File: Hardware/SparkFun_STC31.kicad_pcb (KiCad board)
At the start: 2 copper layers, 25.4 x 25.4 mm, 43 parts, among them J3 Qwiic_RA, J4 I2C, J5 Qwiic_RA, U1 VEML7700-TT

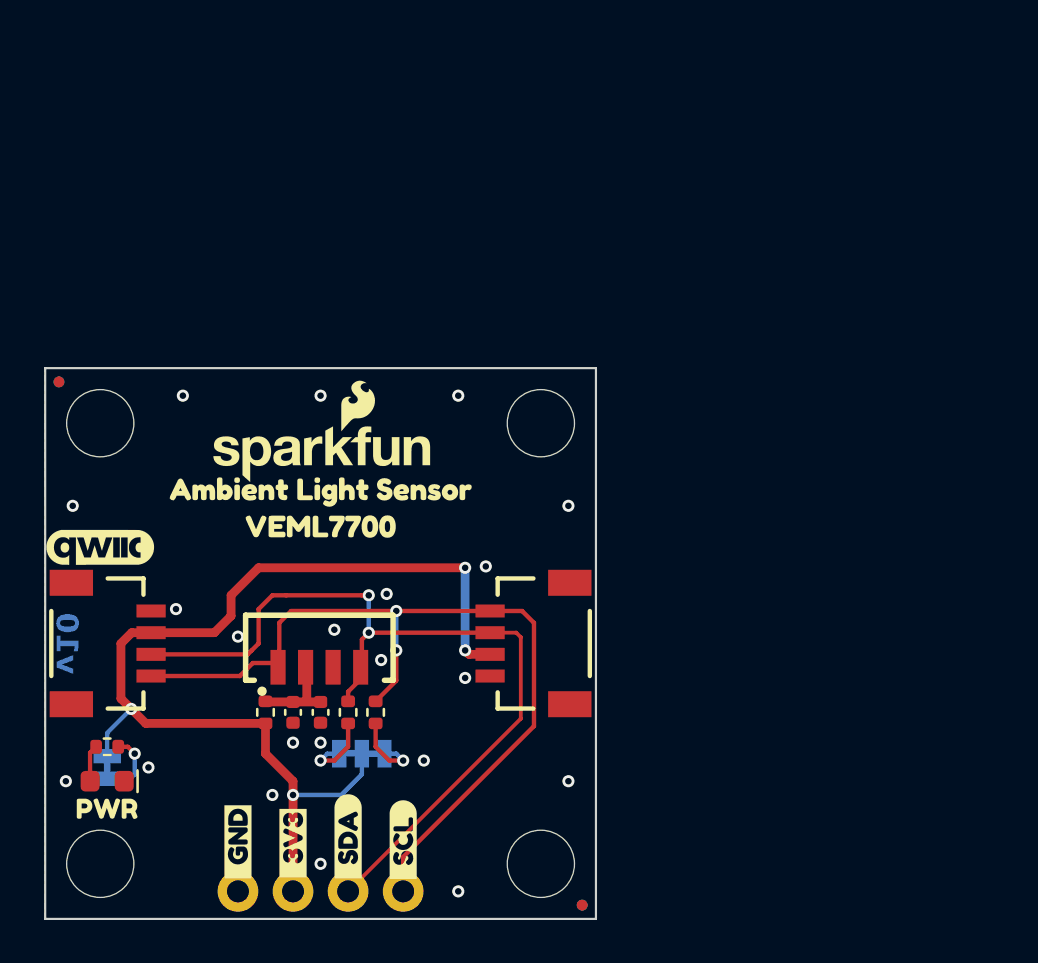
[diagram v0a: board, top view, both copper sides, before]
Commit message: Cleans out the PCB
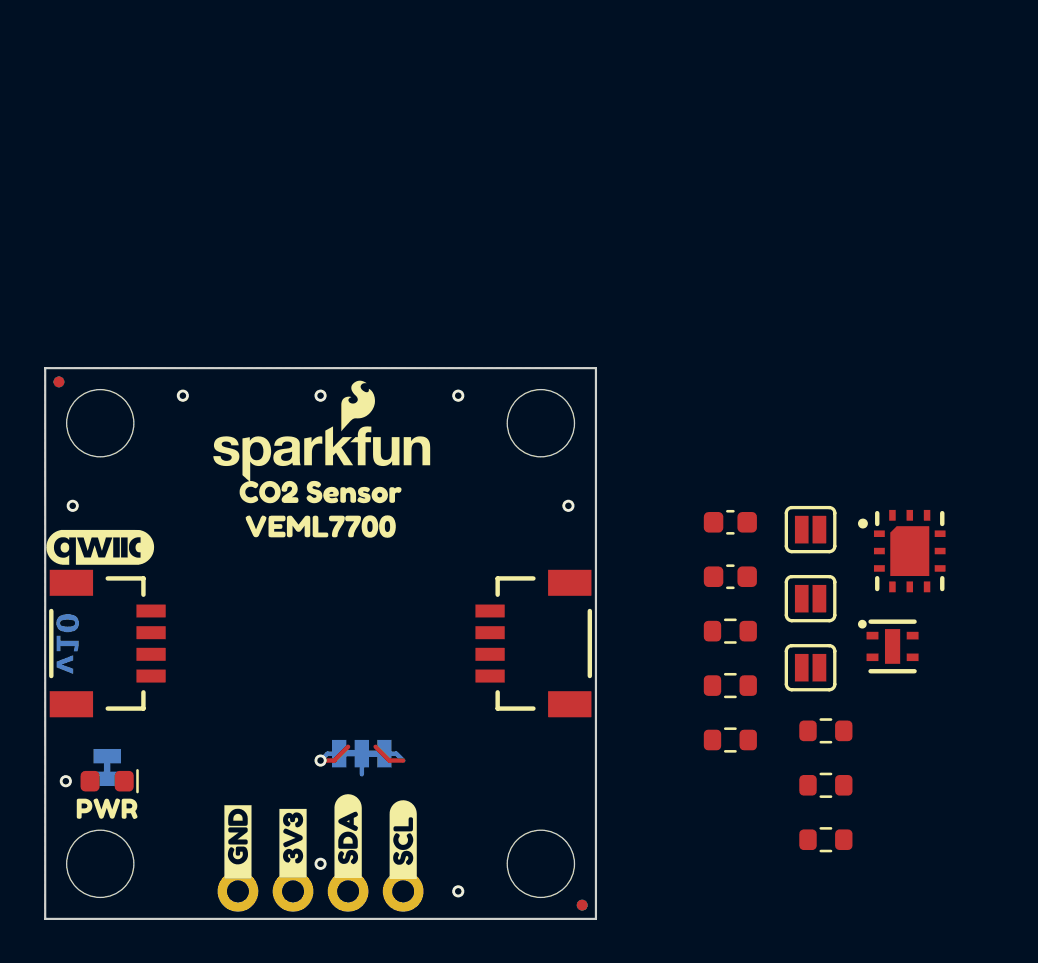
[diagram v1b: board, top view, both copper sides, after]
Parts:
- removed C2: 0.1uF, SparkFun-Capacitor:C_0402_1005Metric
- removed R2, R6: 2.2k, SparkFun-Resistor:R_0402_1005Metric
- removed R3: 4.7k, SparkFun-Resistor:R_0402_1005Metric
- removed kibuzzard-680A7834 (x2): G***, kibuzzard-680A7834
- removed the kibuzzard-680A784B at (136.0, 92.7)
- added C3: 0.1uF, SparkFun-Capacitor:C_0603_1608Metric, F.Cu at (154.9, 95.0)
- added JP3: 0x2A, SparkFun-Jumper:Jumper_2_NO, F.Cu at (158.6, 92.9)
- added JP4: 0x2B, SparkFun-Jumper:Jumper_2_NO, F.Cu at (158.6, 96.0)
- added JP5: 0x2C, SparkFun-Jumper:Jumper_2_NO, F.Cu at (158.6, 99.2)
- added R4: 1k, SparkFun-Resistor:R_0603_1608Metric, F.Cu at (154.9, 100.0)
- added R5: 10k, SparkFun-Resistor:R_0603_1608Metric, F.Cu at (154.9, 102.6)
- added R7: 4.7k, SparkFun-Resistor:R_0603_1608Metric, F.Cu at (159.3, 102.1)
- added R8: 4.7k, SparkFun-Resistor:R_0603_1608Metric, F.Cu at (159.3, 104.6)
- added R9: 4.7k, SparkFun-Resistor:R_0603_1608Metric, F.Cu at (159.3, 107.2)
- added U2: SHTC3, SparkFun-Sensor:SHTC3, F.Cu at (162.3, 98.2)
- added kibuzzard-68139425: G***, kibuzzard-68139425, F.Cu at (136.0, 91.1)
- C1: value 2.2uF -> 0.1uF; footprint SparkFun-Capacitor:C_0402_1005Metric -> SparkFun-Capacitor:C_0603_1608Metric
- R1: value 4.7 -> 3.3k; footprint SparkFun-Resistor:R_0402_1005Metric -> SparkFun-Resistor:R_0603_1608Metric
- U1: value VEML7700-TT -> STC31; footprint SparkFun-Sensor:VEML7700-TT -> SparkFun-Sensor:STC31
- moved U1 27.5 mm to (163.1, 93.8)
- moved C1 22.0 mm to (154.9, 92.5), turned to 0 degrees
- moved R1 21.8 mm to (154.9, 97.5), turned to 0 degrees
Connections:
- C1 pad 1: Net-(U1-VDD) -> 3.3V
- R1 pad 1: Net-(U1-VDD) -> 3.3V
- R1 pad 2: 3.3V -> Net-(JP4-A)
- U1 pad 1: SCL -> GND
- U1 pad 2: Net-(U1-VDD) -> (no net)
- U1 pad 3: GND -> ADDR
- U1 pad 4: SDA -> SCL
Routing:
- net 3.3V: track 48.2 -> 0.95 mm, vias 4 -> 0
- net SCL: track 39.8 -> 0.00 mm, vias 2 -> 0
- net SDA: track 39.6 -> 0.00 mm, vias 2 -> 0
- net Net-(U1-VDD): track 4.19 -> 0.00 mm
- net Net-(JP1-A): track 3.20 -> 0.00 mm, vias 1 -> 0
- net Net-(D1-A): track 1.70 -> 0.00 mm
- net Net-(JP2-C): track 3.61 -> 2.53 mm
- net Net-(JP2-A): track 3.61 -> 2.53 mm, vias 1 -> 0
- net GND: vias 21 -> 8

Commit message: Places parts within the board's outline
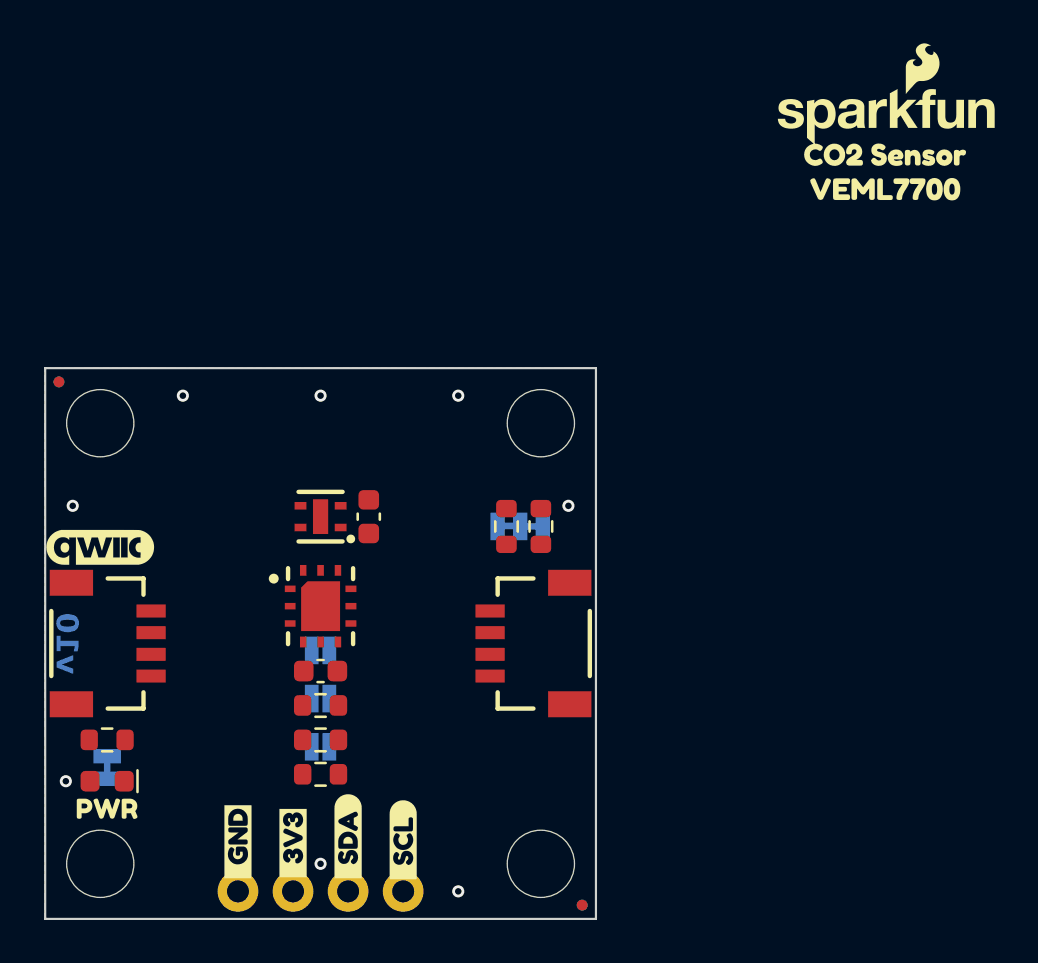
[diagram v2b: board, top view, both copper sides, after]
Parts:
- JP3, JP4, JP5: moved to B.Cu
- moved R9 33.5 mm to (126.1, 102.6)
- moved kibuzzard-680A784B 30.3 mm to (162.0, 77.2)
- moved kibuzzard-680BA25F 30.3 mm to (162.0, 79.1)
- moved G*** 30.3 mm to (162.0, 73.7) (x2)
- moved kibuzzard-68139425 30.3 mm to (162.0, 75.6)
- moved U1 27.3 mm to (136.0, 96.4)
- moved U2 27.1 mm to (136.0, 92.3), turned to 180 degrees
- moved JP3 23.3 mm to (136.0, 98.4)
- moved JP4 23.1 mm to (136.0, 100.6)
- moved JP5 22.9 mm to (136.0, 102.9)
- moved C1 20.1 mm to (136.0, 99.4)
- moved R1 19.6 mm to (136.0, 102.6)
- moved R4 19.3 mm to (136.0, 104.1)
- moved R5 19.0 mm to (136.0, 101.0)
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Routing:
- net Net-(JP2-A): track 2.53 -> 0.00 mm
- net Net-(JP2-C): track 2.53 -> 0.00 mm, vias 1 -> 0
- net 3.3V: track 0.95 -> 0.00 mm

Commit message: Attempts to add some milling
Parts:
- removed kibuzzard-67BF7CAB: G***, kibuzzard-67BF7CAB
- removed kibuzzard-67BF7ED9: G***, kibuzzard-67BF7ED9
- added kibuzzard-681398D9: G***, kibuzzard-681398D9, B.Cu at (134.7, 107.3)
- added kibuzzard-681398E8: G***, kibuzzard-681398E8, F.Cu at (134.7, 107.3)
- moved C3 0.45 mm to (138.2, 92.7)
- moved U2 0.45 mm to (136.0, 92.7)
